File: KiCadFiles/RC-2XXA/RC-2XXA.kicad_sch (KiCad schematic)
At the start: 282 parts

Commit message: Refactor KiCad project files for RC-2XXA: streamline net connections in PCB, adjust solder mask clearance in project settings, and add new connector symbols in schematic. Enhance error handling for undefined net classes.
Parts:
- removed D1, D10, D11, D12, D13, D14, D15, D16, D17, D18, D19, D2, D20, D21, D22, D23, D24, D3, D4, D43, D44, D45, D5, D6, D66, D67, D68, D7, D8, D9, D90, D91, D92: 1N4148, Diode_SMD:D_SOD-323_HandSoldering, symbol Device:D
- removed MX1, MX10, MX11, MX12, MX13, MX14, MX15, MX16, MX17, MX18, MX19, MX2, MX20, MX21, MX22, MX23, MX24, MX3, MX4, MX43, MX44, MX45, MX5, MX6, MX66, MX67, MX68, MX7, MX8, MX9, MX90, MX91, MX92: MX_SW_solder, My-Fi Footprints:SW_MX_1u, symbol PCM_marbastlib-mx:MX_SW_solder
- added C1: 4.7n, Capacitor_SMD:C_0402_1005Metric, symbol Device:C_Small
- added C10 (x2): 1uF, Capacitor_SMD:C_0402_1005Metric, symbol Device:C_Small
- added C11: 4.7uF/10V, Capacitor_SMD:C_0402_1005Metric, symbol Device:C_Small
- added C12: 100nF, Capacitor_SMD:C_0402_1005Metric, symbol Device:C_Small
- added C2, C3, C4, C5, C6: 100nF, Capacitor_SMD:C_0402_1005Metric, symbol Device:C
- added C7: 10uF, Capacitor_SMD:C_0402_1005Metric, symbol Device:C
- added C8, C9: 1uF, Capacitor_SMD:C_0402_1005Metric, symbol Device:C
- added F1: 500mA, Fuse:Fuse_1206_3216Metric, symbol Device:Polyfuse_Small
- added J1: Conn_01x04_Pin, Connector_JST:JST_SH_SM04B-SRSS-TB_1x04-1MP_P1.00mm_Horizontal, symbol Connector:Conn_01x04_Pin
- added J2: Conn_01x01_Pin, TestPoint:TestPoint_THTPad_2.0x2.0mm_Drill1.0mm, symbol Connector:Conn_01x01_Pin
- added LED1, LED2, LED4, LED6: LED, My-Fi Footprints:DIP_LED_MX_3mm, symbol Device:LED
- added LED3, LED5: LED, My-Fi Footprints:CAPS_LED_MX_3mm, symbol Device:LED
- added R1: 1M, Resistor_SMD:R_0402_1005Metric, symbol Device:R_Small
- added R2, R3, R4, R6: 220, Resistor_SMD:R_0402_1005Metric, symbol Device:R_Small
- added R5, R8: 10k, Resistor_SMD:R_0402_1005Metric, symbol Device:R
- added R9: 39R, Resistor_SMD:R_0402_1005Metric, symbol Device:R
- added SW1, SW2: SW_DPST_x2, Button_Switch_SMD:SW_Push_1P1T_XKB_TS-1187A, symbol Switch:SW_DPST_x2
- added U1: SRV05-4, Package_TO_SOT_SMD:SOT-23-6, symbol Power_Protection:SRV05-4
- added U2: STM32F072CBTx, Package_QFP:LQFP-48_7x7mm_P0.5mm, symbol MCU_ST_STM32F0:STM32F072CBTx
- added U3: XC6206PxxxMR, Package_TO_SOT_SMD:SOT-23-3, symbol Regulator_Linear:XC6206PxxxMR
- added U4: TLV74318PDBVR, Package_TO_SOT_SMD:SOT-23-5, symbol pmw3360:TLV74318PDBVR
- added U5: PMW3360DM-T2QU, Library:TrackballHolder_34mm, symbol pmw3360:PMW3360DM-T2QU
- D1: renamed from D25; footprint Diode_SMD:D_SOD-323_HandSoldering -> Diode_SMD:D_SOD-123
- D10: renamed from D34; footprint Diode_SMD:D_SOD-323_HandSoldering -> Diode_SMD:D_SOD-123
- D100: renamed from D133; footprint Diode_SMD:D_SOD-323_HandSoldering -> Diode_SMD:D_SOD-123
- D101: renamed from D134; footprint Diode_SMD:D_SOD-323_HandSoldering -> Diode_SMD:D_SOD-123
- D102: renamed from D135; footprint Diode_SMD:D_SOD-323_HandSoldering -> Diode_SMD:D_SOD-123
- D103: renamed from D136; footprint Diode_SMD:D_SOD-323_HandSoldering -> Diode_SMD:D_SOD-123
- D104: renamed from D137; footprint Diode_SMD:D_SOD-323_HandSoldering -> Diode_SMD:D_SOD-123
- D11: renamed from D35; footprint Diode_SMD:D_SOD-323_HandSoldering -> Diode_SMD:D_SOD-123
- D12: renamed from D36; footprint Diode_SMD:D_SOD-323_HandSoldering -> Diode_SMD:D_SOD-123
- D13: renamed from D37; footprint Diode_SMD:D_SOD-323_HandSoldering -> Diode_SMD:D_SOD-123
- D14: renamed from D38; footprint Diode_SMD:D_SOD-323_HandSoldering -> Diode_SMD:D_SOD-123
- D15: renamed from D39; footprint Diode_SMD:D_SOD-323_HandSoldering -> Diode_SMD:D_SOD-123
- D16: renamed from D40; footprint Diode_SMD:D_SOD-323_HandSoldering -> Diode_SMD:D_SOD-123
- D17: renamed from D41; footprint Diode_SMD:D_SOD-323_HandSoldering -> Diode_SMD:D_SOD-123
- D18: renamed from D42; footprint Diode_SMD:D_SOD-323_HandSoldering -> Diode_SMD:D_SOD-123
- D19: renamed from D46; footprint Diode_SMD:D_SOD-323_HandSoldering -> Diode_SMD:D_SOD-123
- D2: renamed from D26; footprint Diode_SMD:D_SOD-323_HandSoldering -> Diode_SMD:D_SOD-123
- D20: renamed from D47; footprint Diode_SMD:D_SOD-323_HandSoldering -> Diode_SMD:D_SOD-123
- D21: renamed from D48; footprint Diode_SMD:D_SOD-323_HandSoldering -> Diode_SMD:D_SOD-123
- D22: renamed from D49; footprint Diode_SMD:D_SOD-323_HandSoldering -> Diode_SMD:D_SOD-123
- D23: renamed from D50; footprint Diode_SMD:D_SOD-323_HandSoldering -> Diode_SMD:D_SOD-123
- D24: renamed from D51; footprint Diode_SMD:D_SOD-323_HandSoldering -> Diode_SMD:D_SOD-123
- D25: renamed from D52; footprint Diode_SMD:D_SOD-323_HandSoldering -> Diode_SMD:D_SOD-123
- D26: renamed from D53; footprint Diode_SMD:D_SOD-323_HandSoldering -> Diode_SMD:D_SOD-123
- D27: renamed from D54; footprint Diode_SMD:D_SOD-323_HandSoldering -> Diode_SMD:D_SOD-123
- D28: renamed from D55; footprint Diode_SMD:D_SOD-323_HandSoldering -> Diode_SMD:D_SOD-123
- D29: renamed from D56; footprint Diode_SMD:D_SOD-323_HandSoldering -> Diode_SMD:D_SOD-123
- D3: renamed from D27; footprint Diode_SMD:D_SOD-323_HandSoldering -> Diode_SMD:D_SOD-123
- D30: renamed from D57; footprint Diode_SMD:D_SOD-323_HandSoldering -> Diode_SMD:D_SOD-123
- D31: renamed from D58; footprint Diode_SMD:D_SOD-323_HandSoldering -> Diode_SMD:D_SOD-123
- D32: renamed from D59; footprint Diode_SMD:D_SOD-323_HandSoldering -> Diode_SMD:D_SOD-123
- D33: renamed from D60; footprint Diode_SMD:D_SOD-323_HandSoldering -> Diode_SMD:D_SOD-123
- D34: renamed from D61; footprint Diode_SMD:D_SOD-323_HandSoldering -> Diode_SMD:D_SOD-123
- D35: renamed from D62; footprint Diode_SMD:D_SOD-323_HandSoldering -> Diode_SMD:D_SOD-123
- D36: renamed from D63; footprint Diode_SMD:D_SOD-323_HandSoldering -> Diode_SMD:D_SOD-123
- D37: renamed from D64; footprint Diode_SMD:D_SOD-323_HandSoldering -> Diode_SMD:D_SOD-123
- D38: renamed from D65; footprint Diode_SMD:D_SOD-323_HandSoldering -> Diode_SMD:D_SOD-123
- D39: renamed from D69; footprint Diode_SMD:D_SOD-323_HandSoldering -> Diode_SMD:D_SOD-123
- D4: renamed from D28; footprint Diode_SMD:D_SOD-323_HandSoldering -> Diode_SMD:D_SOD-123
- D40: renamed from D70; footprint Diode_SMD:D_SOD-323_HandSoldering -> Diode_SMD:D_SOD-123
- D41: renamed from D71; footprint Diode_SMD:D_SOD-323_HandSoldering -> Diode_SMD:D_SOD-123
- D42: renamed from D72; footprint Diode_SMD:D_SOD-323_HandSoldering -> Diode_SMD:D_SOD-123
- D43: renamed from D73; footprint Diode_SMD:D_SOD-323_HandSoldering -> Diode_SMD:D_SOD-123
- D44: renamed from D74; footprint Diode_SMD:D_SOD-323_HandSoldering -> Diode_SMD:D_SOD-123
- D45: renamed from D75; footprint Diode_SMD:D_SOD-323_HandSoldering -> Diode_SMD:D_SOD-123
- D46: renamed from D76; footprint Diode_SMD:D_SOD-323_HandSoldering -> Diode_SMD:D_SOD-123
- D47: renamed from D77; footprint Diode_SMD:D_SOD-323_HandSoldering -> Diode_SMD:D_SOD-123
- D48: renamed from D78; footprint Diode_SMD:D_SOD-323_HandSoldering -> Diode_SMD:D_SOD-123
- D49: renamed from D79; footprint Diode_SMD:D_SOD-323_HandSoldering -> Diode_SMD:D_SOD-123
- D5: renamed from D29; footprint Diode_SMD:D_SOD-323_HandSoldering -> Diode_SMD:D_SOD-123
- D50: renamed from D80; footprint Diode_SMD:D_SOD-323_HandSoldering -> Diode_SMD:D_SOD-123
- D51: renamed from D81; footprint Diode_SMD:D_SOD-323_HandSoldering -> Diode_SMD:D_SOD-123
- D52: renamed from D82; footprint Diode_SMD:D_SOD-323_HandSoldering -> Diode_SMD:D_SOD-123
- D53: renamed from D83; footprint Diode_SMD:D_SOD-323_HandSoldering -> Diode_SMD:D_SOD-123
- D54: renamed from D84; footprint Diode_SMD:D_SOD-323_HandSoldering -> Diode_SMD:D_SOD-123
- D55: renamed from D85; footprint Diode_SMD:D_SOD-323_HandSoldering -> Diode_SMD:D_SOD-123
- D56: renamed from D86; footprint Diode_SMD:D_SOD-323_HandSoldering -> Diode_SMD:D_SOD-123
- D57: renamed from D87; footprint Diode_SMD:D_SOD-323_HandSoldering -> Diode_SMD:D_SOD-123
- D58: renamed from D88; footprint Diode_SMD:D_SOD-323_HandSoldering -> Diode_SMD:D_SOD-123
- D59: renamed from D89; footprint Diode_SMD:D_SOD-323_HandSoldering -> Diode_SMD:D_SOD-123
- D6: renamed from D30; footprint Diode_SMD:D_SOD-323_HandSoldering -> Diode_SMD:D_SOD-123
- D60: renamed from D93; footprint Diode_SMD:D_SOD-323_HandSoldering -> Diode_SMD:D_SOD-123
- D61: renamed from D94; footprint Diode_SMD:D_SOD-323_HandSoldering -> Diode_SMD:D_SOD-123
- D62: renamed from D95; footprint Diode_SMD:D_SOD-323_HandSoldering -> Diode_SMD:D_SOD-123
- D63: renamed from D96; footprint Diode_SMD:D_SOD-323_HandSoldering -> Diode_SMD:D_SOD-123
- D64: renamed from D97; footprint Diode_SMD:D_SOD-323_HandSoldering -> Diode_SMD:D_SOD-123
- D65: renamed from D98; footprint Diode_SMD:D_SOD-323_HandSoldering -> Diode_SMD:D_SOD-123
- D66: renamed from D99; footprint Diode_SMD:D_SOD-323_HandSoldering -> Diode_SMD:D_SOD-123
- D67: renamed from D100; footprint Diode_SMD:D_SOD-323_HandSoldering -> Diode_SMD:D_SOD-123
- D68: renamed from D101; footprint Diode_SMD:D_SOD-323_HandSoldering -> Diode_SMD:D_SOD-123
- D69: renamed from D102; footprint Diode_SMD:D_SOD-323_HandSoldering -> Diode_SMD:D_SOD-123
- D7: renamed from D31; footprint Diode_SMD:D_SOD-323_HandSoldering -> Diode_SMD:D_SOD-123
- D70: renamed from D103; footprint Diode_SMD:D_SOD-323_HandSoldering -> Diode_SMD:D_SOD-123
- D71: renamed from D104; footprint Diode_SMD:D_SOD-323_HandSoldering -> Diode_SMD:D_SOD-123
- D72: renamed from D105; footprint Diode_SMD:D_SOD-323_HandSoldering -> Diode_SMD:D_SOD-123
- D73: renamed from D106; footprint Diode_SMD:D_SOD-323_HandSoldering -> Diode_SMD:D_SOD-123
- D74: renamed from D107; footprint Diode_SMD:D_SOD-323_HandSoldering -> Diode_SMD:D_SOD-123
- D75: renamed from D108; footprint Diode_SMD:D_SOD-323_HandSoldering -> Diode_SMD:D_SOD-123
- D76: renamed from D109; footprint Diode_SMD:D_SOD-323_HandSoldering -> Diode_SMD:D_SOD-123
- D77: renamed from D110; footprint Diode_SMD:D_SOD-323_HandSoldering -> Diode_SMD:D_SOD-123
- D78: renamed from D111; footprint Diode_SMD:D_SOD-323_HandSoldering -> Diode_SMD:D_SOD-123
- D79: renamed from D112; footprint Diode_SMD:D_SOD-323_HandSoldering -> Diode_SMD:D_SOD-123
- D8: renamed from D32; footprint Diode_SMD:D_SOD-323_HandSoldering -> Diode_SMD:D_SOD-123
- D80: renamed from D113; footprint Diode_SMD:D_SOD-323_HandSoldering -> Diode_SMD:D_SOD-123
- D81: renamed from D114; footprint Diode_SMD:D_SOD-323_HandSoldering -> Diode_SMD:D_SOD-123
- D82: renamed from D115; footprint Diode_SMD:D_SOD-323_HandSoldering -> Diode_SMD:D_SOD-123
- D83: renamed from D116; footprint Diode_SMD:D_SOD-323_HandSoldering -> Diode_SMD:D_SOD-123
- D84: renamed from D117; footprint Diode_SMD:D_SOD-323_HandSoldering -> Diode_SMD:D_SOD-123
- D85: renamed from D118; footprint Diode_SMD:D_SOD-323_HandSoldering -> Diode_SMD:D_SOD-123
- D86: renamed from D119; footprint Diode_SMD:D_SOD-323_HandSoldering -> Diode_SMD:D_SOD-123
- D87: renamed from D120; footprint Diode_SMD:D_SOD-323_HandSoldering -> Diode_SMD:D_SOD-123
- D88: renamed from D121; footprint Diode_SMD:D_SOD-323_HandSoldering -> Diode_SMD:D_SOD-123
- D89: renamed from D122; footprint Diode_SMD:D_SOD-323_HandSoldering -> Diode_SMD:D_SOD-123
- D9: renamed from D33; footprint Diode_SMD:D_SOD-323_HandSoldering -> Diode_SMD:D_SOD-123
- D90: renamed from D123; footprint Diode_SMD:D_SOD-323_HandSoldering -> Diode_SMD:D_SOD-123
- D91: renamed from D124; footprint Diode_SMD:D_SOD-323_HandSoldering -> Diode_SMD:D_SOD-123
- D92: renamed from D125; footprint Diode_SMD:D_SOD-323_HandSoldering -> Diode_SMD:D_SOD-123
- D93: renamed from D126; footprint Diode_SMD:D_SOD-323_HandSoldering -> Diode_SMD:D_SOD-123
- D94: renamed from D127; footprint Diode_SMD:D_SOD-323_HandSoldering -> Diode_SMD:D_SOD-123
- D95: renamed from D128; footprint Diode_SMD:D_SOD-323_HandSoldering -> Diode_SMD:D_SOD-123
- D96: renamed from D129; footprint Diode_SMD:D_SOD-323_HandSoldering -> Diode_SMD:D_SOD-123
- D97: renamed from D130; footprint Diode_SMD:D_SOD-323_HandSoldering -> Diode_SMD:D_SOD-123
- D98: renamed from D131; footprint Diode_SMD:D_SOD-323_HandSoldering -> Diode_SMD:D_SOD-123
- D99: renamed from D132; footprint Diode_SMD:D_SOD-323_HandSoldering -> Diode_SMD:D_SOD-123
- renumbered MX25 to MX1, MX34 to MX10, MX133 to MX100, MX134 to MX101, MX135 to MX102, MX136 to MX103, MX137 to MX104, MX35 to MX11, MX36 to MX12, MX37 to MX13, MX38 to MX14, MX39 to MX15, MX40 to MX16, MX41 to MX17, MX42 to MX18, MX46 to MX19, MX26 to MX2, MX47 to MX20, MX48 to MX21, MX49 to MX22, MX50 to MX23, MX51 to MX24, MX52 to MX25, MX53 to MX26, MX54 to MX27, MX55 to MX28, MX56 to MX29, MX27 to MX3, MX57 to MX30, MX58 to MX31, MX59 to MX32, MX60 to MX33, MX61 to MX34, MX62 to MX35, MX63 to MX36, MX64 to MX37, MX65 to MX38, MX69 to MX39, MX28 to MX4, MX70 to MX40, MX71 to MX41, MX72 to MX42, MX73 to MX43, MX74 to MX44, MX75 to MX45, MX76 to MX46, MX77 to MX47, MX78 to MX48, MX79 to MX49, MX29 to MX5, MX80 to MX50, MX81 to MX51, MX82 to MX52, MX83 to MX53, MX84 to MX54, MX85 to MX55, MX86 to MX56, MX87 to MX57, MX88 to MX58, MX89 to MX59, MX30 to MX6, MX93 to MX60, MX94 to MX61, MX95 to MX62, MX96 to MX63, MX97 to MX64, MX98 to MX65, MX99 to MX66, MX100 to MX67, MX101 to MX68, MX102 to MX69, MX31 to MX7, MX103 to MX70, MX104 to MX71, MX105 to MX72, MX106 to MX73, MX107 to MX74, MX108 to MX75, MX109 to MX76, MX110 to MX77, MX111 to MX78, MX112 to MX79, MX32 to MX8, MX113 to MX80, MX114 to MX81, MX115 to MX82, MX116 to MX83, MX117 to MX84, MX118 to MX85, MX119 to MX86, MX120 to MX87, MX121 to MX88, MX122 to MX89, MX33 to MX9, MX123 to MX90, MX124 to MX91, MX125 to MX92, MX126 to MX93, MX127 to MX94, MX128 to MX95, MX129 to MX96, MX130 to MX97, MX131 to MX98, MX132 to MX99, S134 to S101, S41 to S17, S73 to S43, S89 to S59, S100 to S67, S113 to S80, S122 to S89, S127 to S94
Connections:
- net COL1: now reaches MX26.1
- net COL1: now also MX4.1, MX48.1, MX68.1, U2.21 (PB10)
- net COL16: now reaches MX83.1
- net COL16: now also MX98.1, U2.3 (PC14)
- net COL6: now reaches MX53.1
- net COL6: now also MX31.1, MX73.1, MX9.1, MX94.1, U2.13 (PA3)
- net COL0: now reaches MX3.1
- net COL0: now also MX25.1, MX46.1, MX66.1, MX92.1, U2.22 (PB11)
- net COL7: now reaches MX10.1
- net COL7: now also MX32.1, MX54.1, MX74.1, U2.28 (PB15)
- net COL10: now reaches MX57.1
- net COL10: now also MX13.1, MX35.1, MX77.1, U2.25 (PB12)
- net COL11: now reaches MX36.1
- net COL11: now also MX14.1, MX58.1, MX78.1, MX95.1, U2.12 (PA2)
- net COL3: now reaches MX28.1
- net COL3: now also MX50.1, MX6.1, MX70.1, MX93.1, U2.19 (PB1)
- net COL9: now reaches MX56.1
- net COL9: now also MX12.1, MX34.1, MX76.1, U2.26 (PB13)
- net COL12: now reaches MX59.1
- net COL12: now also MX15.1, MX37.1, MX79.1, U2.11 (PA1)
- net COL8: now reaches MX33.1
- net COL8: now also MX11.1, MX55.1, MX75.1, U2.27 (PB14)
- net COL19: now reaches MX102.1
- net COL19: now also MX20.1, MX40.1, MX61.1, MX86.1
- net COL13: now reaches MX96.1
- net COL13: now also MX16.1, MX38.1, MX81.1, U2.6 (PF1)
- net COL15: now reaches MX82.1
- net COL15: now also MX97.1, U2.4 (PC15)
- net COL21: now reaches MX22.1
- net COL21: now also MX104.1, MX42.1, MX43.1, MX63.1, MX88.1, MX89.1
- net COL18: now reaches MX100.1
- net COL18: now also MX19.1, MX39.1, MX60.1, MX85.1
- net COL17: now reaches MX99.1
- net COL17: now also MX84.1, U2.2 (PC13)
- net COL2: now reaches MX49.1
- net COL2: now also MX27.1, MX5.1, MX69.1, U2.20 (PB2)
- net COL5: now reaches MX72.1
- net COL5: now also MX30.1, MX52.1, MX8.1
- net COL4: now reaches MX29.1
- net COL4: now also MX51.1, MX7.1, MX71.1
- net COL20: now reaches MX87.1
- net COL20: now also MX103.1, MX21.1, MX41.1, MX62.1
- net COL14: now reaches MX18.1
- net COL14: now also U2.5 (PF0)
- new net: LED3.2 (A), LED4.2 (A), R4.2
- new net: LED1.2 (A), R2.2
- new net: C11.1, C12.1, U5.3 (VDDPIX)
- new net: LED5.2 (A), LED6.2 (A), R6.2
- new net: R9.1, U5.15 (LED_P)
- new net: LED2.2 (A), R3.2
- new net +3V3: C10.1, C3.1, C4.1, C5.1, C6.1, C7.1, C9.1, R8.1, SW2.2 (B), U2.1 (VBAT), U2.24 (VDD), U2.36 (VDDIO2), U2.48 (VDD), U2.9 (VDDA), U3.2 (VO), U4.1 (IN), U4.3 (EN), U5.5 (VDDIO)
- new net +5V: C8.1, F1.2, U1.5 (VP), U3.3 (VI)
- new net BOOT-1: R5.1, SW2.1 (A), U2.44 (BOOT0)
- new net CAPLED: R4.1, U2.18 (PB0)
- new net CS: U2.14 (PA4), U5.13 (~{CS})
- new net DN: J1.2 (Pin_2), U1.4 (IO3), U2.32 (PA11)
- new net DP: J1.3 (Pin_3), U1.6 (IO4), U2.33 (PA12)
- new net ESCLED: R2.1, U2.41 (PB5)
- new net GND: C1.2, C10.2, C10.2, C11.2, C12.2, C2.2, C3.2, C4.2, C5.2, C6.2, C7.2, C8.2, C9.2, J1.4 (Pin_4), LED1.1 (K), LED2.1 (K), LED3.1 (K), LED4.1 (K), LED5.1 (K), LED6.1 (K), R1.2, R5.2, SW1.2 (B), U1.2 (VN), U2.23 (VSS), U2.35 (VSS), U2.47 (VSS), U2.8 (VSSA), U3.1 (GND), U4.2 (GND), U5.8 (GND)
- new net GNDREF: C1.1, J2.1 (Pin_1), R1.1
- new net MISO: R8.2, U2.16 (PA6), U5.12 (MISO)
- new net MOSI: U2.17 (PA7), U5.11 (MOSI)
- new net NUMLED: R6.1
- new net ROW0: U2.37 (PA14)
- new net ROW1: U2.38 (PA15)
- new net ROW2: U2.39 (PB3)
- new net ROW3: U2.40 (PB4)
- new net RST-1: C2.1, SW1.1 (A), U2.7 (NRST)
- new net SCLK: U2.15 (PA5), U5.10 (SCLK)
- new net SCLLED: R3.1, U2.42 (PB6)
- new net VBUS: F1.1, J1.1 (Pin_1)
- new net VDD_TR: C10.1, R9.2, U4.5 (OUT), U5.4 (VDD)
- no-connect marks 0 -> 6
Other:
- note added: "Boot Switch"
- note added: "Capslock LED"
- note added: "Decoupling Capacitors"
- note added: "ESC LED"
- note added: "ESD Protect"
- note added: "Fuse"
- note added: "JST Connetor"
- note added: "MCU STM32F072CBT6"
- note added: "Regulator TLV74318PDBVR 3.3V-1.8V"
- note added: "Regulator XC6206 5V-3.3V"
- note added: "Reset Switch"
- note added: "SENSOR PMW3360DM-T2QU"
- note added: "ScollLock LED"
- note added: "Shielding"
- moved on the sheet: D1, D10, D100, D101, D102, D103, D104, D11, D12, D13, D14, D15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

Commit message: Update rectangle positions in RC-2XXA schematic to correct alignment and spacing. Adjust multiple rectangle coordinates for improved layout consistency.
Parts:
- removed R2: 220, Resistor_SMD:R_0402_1005Metric, symbol Device:R_Small
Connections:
- net COL21 is gone; now on net COL20: MX104.1, MX22.1, MX42.1, MX43.1, MX63.1, MX88.1, MX89.1
- net ESCLED is gone; now on net SCLLED: U2.41 (PB5)
- net COL0: now also U2.5 (PF0); no longer U2.22 (PB11)
- net COL1: now also U2.6 (PF1); no longer U2.21 (PB10)
- net COL10: now also U2.45 (PB8); no longer U2.25 (PB12)
- net COL11: now also U2.46 (PB9); no longer U2.12 (PA2)
- net COL12: now also MX1.1, MX2.1, U2.21 (PB10); no longer U2.11 (PA1)
- net COL13: now also MX23.1, MX24.1, U2.22 (PB11); no longer U2.6 (PF1)
- net COL14: now also MX44.1, MX45.1, MX82.1, MX97.1, U2.25 (PB12); no longer U2.5 (PF0)
- net COL15: now also MX64.1, MX65.1, MX83.1, MX98.1, U2.26 (PB13); no longer MX82.1, MX97.1, U2.4 (PC15)
- net COL16: now also MX84.1, MX90.1, MX91.1, MX99.1, U2.27 (PB14); no longer MX83.1, MX98.1, U2.3 (PC14)
- net COL17: now also MX100.1, MX19.1, MX39.1, MX60.1, MX85.1, U2.28 (PB15); no longer MX84.1, MX99.1, U2.2 (PC13)
- net COL18: now also MX102.1, MX20.1, MX40.1, MX61.1, MX86.1, U2.10 (PA0); no longer MX100.1, MX19.1, MX39.1, MX60.1, MX85.1
- net COL19: now also MX103.1, MX21.1, MX41.1, MX62.1, MX87.1, U2.11 (PA1); no longer MX102.1, MX20.1, MX40.1, MX61.1, MX86.1
- net COL2: now also U2.2 (PC13); no longer U2.20 (PB2)
- net COL20: now also U2.12 (PA2); no longer MX103.1, MX21.1, MX41.1, MX62.1, MX87.1
- net COL3: now also U2.3 (PC14); no longer U2.19 (PB1)
- net COL4: now also U2.4 (PC15)
- net COL5: now also U2.20 (PB2)
- net COL6: now also U2.39 (PB3); no longer U2.13 (PA3)
- net COL7: now also U2.40 (PB4); no longer U2.28 (PB15)
- net COL8: now also U2.42 (PB6); no longer U2.27 (PB14)
- net COL9: now also U2.43 (PB7); no longer U2.26 (PB13)
- net NUMLED: now also U2.19 (PB1)
- net ROW0: now also D1.1 (K), D23.1 (K), D44.1 (K), D64.1 (K), D90.1 (K), U2.13 (PA3); no longer U2.37 (PA14)
- net ROW1: now also D2.1 (K), D24.1 (K), D45.1 (K), D65.1 (K), D91.1 (K), U2.29 (PA8); no longer U2.38 (PA15)
- net ROW2: now also D10.1 (K), D11.1 (K), D12.1 (K), D13.1 (K), D14.1 (K), D15.1 (K), D16.1 (K), D17.1 (K), D18.1 (K), D19.1 (K), D20.1 (K), D21.1 (K), D22.1 (K), D3.1 (K), D4.1 (K), D5.1 (K), D6.1 (K), D7.1 (K), D8.1 (K), D9.1 (K), U2.30 (PA9); no longer U2.39 (PB3)
- net ROW3: now also D25.1 (K), D26.1 (K), D27.1 (K), D28.1 (K), D29.1 (K), D30.1 (K), D31.1 (K), D32.1 (K), D33.1 (K), D34.1 (K), D35.1 (K), D36.1 (K), D37.1 (K), D38.1 (K), D39.1 (K), D40.1 (K), D41.1 (K), D42.1 (K), U2.31 (PA10); no longer U2.40 (PB4)
- net SCLLED: no longer U2.42 (PB6)
- net ROW6: now reaches D96.1 (K)
- net ROW6: now also D100.1 (K), D101.1 (K), D102.1 (K), D103.1 (K), D104.1 (K), D92.1 (K), D93.1 (K), D94.1 (K), D95.1 (K), D97.1 (K), D98.1 (K), D99.1 (K), U2.38 (PA15)
- net at LED1.2 (A): now also LED2.2 (A), R3.2
- net ROW4: now reaches U2.34 (PA13)
- net ROW4: now also D46.1 (K), D47.1 (K), D48.1 (K), D49.1 (K), D50.1 (K), D51.1 (K), D52.1 (K), D53.1 (K), D54.1 (K), D55.1 (K), D56.1 (K), D57.1 (K), D58.1 (K), D59.1 (K), D60.1 (K), D61.1 (K), D62.1 (K), D63.1 (K)
- net ROW5: now reaches D86.1 (K)
- net ROW5: now also D66.1 (K), D67.1 (K), D68.1 (K), D69.1 (K), D70.1 (K), D71.1 (K), D72.1 (K), D73.1 (K), D74.1 (K), D75.1 (K), D76.1 (K), D77.1 (K), D78.1 (K), D79.1 (K), D80.1 (K), D81.1 (K), D82.1 (K), D83.1 (K), D84.1 (K), D85.1 (K), D87.1 (K), D88.1 (K), U2.37 (PA14)
- no-connect marks 6 -> 5
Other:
- note removed: "ESC LED"
- moved on the sheet: D1, D10, D100, D101, D102, D103, D104, D11, D12, D13, D14, D15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

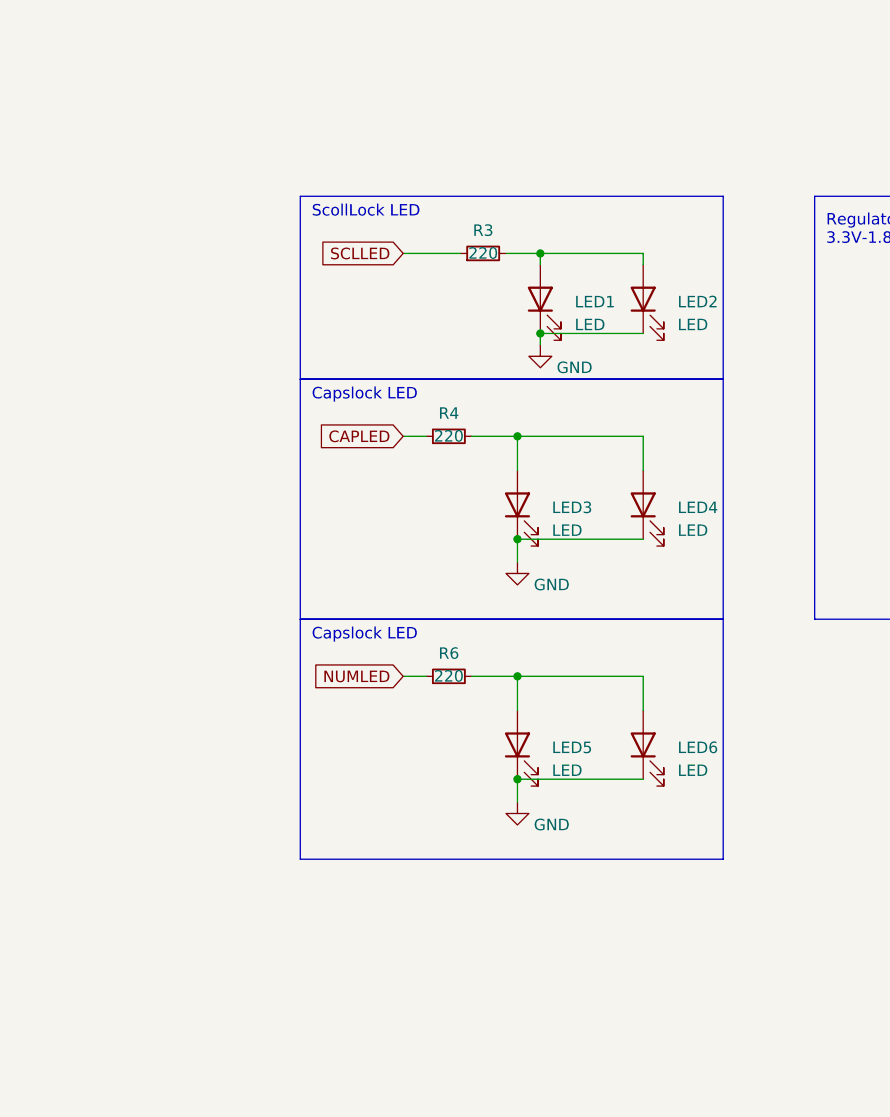
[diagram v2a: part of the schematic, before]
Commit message: Update RC-2XXA KiCad files: adjust footprint properties, correct rectangle positions in schematic, and enhance error handling for pin connections. Remove unnecessary junctions and wires for improved clarity.
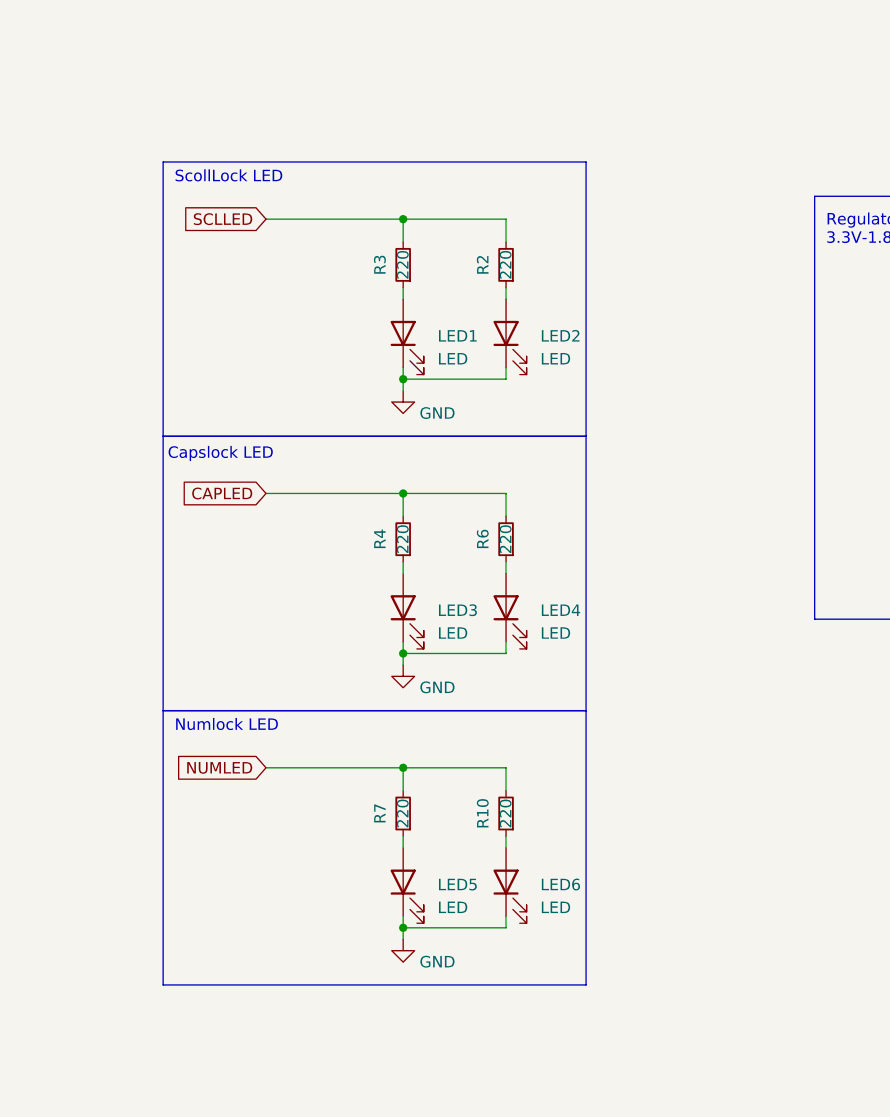
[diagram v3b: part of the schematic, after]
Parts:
- added R10, R2, R7: 220, Resistor_SMD:R_0402_1005Metric, symbol Device:R_Small
- LED3, LED5: footprint My-Fi Footprints:CAPS_LED_MX_3mm -> My-Fi Footprints:DIP_LED_MX_3mm
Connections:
- net CAPLED: now also R4.2, R6.2; no longer R4.1
- net NUMLED: now also R10.2, R7.2; no longer R6.1
- net SCLLED: now also R3.2, R2.2; no longer R3.1
- new net: LED4.2 (A), R6.1
- new net: LED5.2 (A), R7.1
- new net: LED3.2 (A), R4.1
- new net: LED1.2 (A), R3.1
- new net: LED6.2 (A), R10.1
- new net: LED2.2 (A), R2.1
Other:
- note added: "Numlock LED"
- moved on the sheet: LED1, LED2, R3

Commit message: Add Zener diode symbol to RC-2XXA schematic, update component references and footprints for capacitors and resistors, and correct wire connections for improved circuit clarity.
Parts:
- added D206: SMF6.0A, acheron_Components:D_SOD-123, symbol Device:D_Zener
- C1: value 4.7n -> 4.7nF; footprint Capacitor_SMD:C_0402_1005Metric -> Capacitor_SMD:C_0805_2012Metric_Pad1.18x1.45mm_HandSolder
- C10: renamed from C6; footprint Capacitor_SMD:C_0402_1005Metric -> Capacitor_SMD:C_0805_2012Metric_Pad1.18x1.45mm_HandSolder
- C11: renamed from C7; footprint Capacitor_SMD:C_0402_1005Metric -> Capacitor_SMD:C_0805_2012Metric_Pad1.18x1.45mm_HandSolder
- C12: renamed from C8; footprint Capacitor_SMD:C_0402_1005Metric -> Capacitor_SMD:C_0805_2012Metric_Pad1.18x1.45mm_HandSolder
- C13: renamed from C9; footprint Capacitor_SMD:C_0402_1005Metric -> Capacitor_SMD:C_0805_2012Metric_Pad1.18x1.45mm_HandSolder
- C2, C3: renamed from C10; footprint Capacitor_SMD:C_0402_1005Metric -> Capacitor_SMD:C_0805_2012Metric_Pad1.18x1.45mm_HandSolder
- C4: renamed from C11; footprint Capacitor_SMD:C_0402_1005Metric -> Capacitor_SMD:C_0805_2012Metric_Pad1.18x1.45mm_HandSolder
- C5: renamed from C12; footprint Capacitor_SMD:C_0402_1005Metric -> Capacitor_SMD:C_0805_2012Metric_Pad1.18x1.45mm_HandSolder
- C6: renamed from C2; footprint Capacitor_SMD:C_0402_1005Metric -> Capacitor_SMD:C_0805_2012Metric_Pad1.18x1.45mm_HandSolder
- C7: renamed from C3; footprint Capacitor_SMD:C_0402_1005Metric -> Capacitor_SMD:C_0805_2012Metric_Pad1.18x1.45mm_HandSolder
- C8: renamed from C4; footprint Capacitor_SMD:C_0402_1005Metric -> Capacitor_SMD:C_0805_2012Metric_Pad1.18x1.45mm_HandSolder
- C9: renamed from C5; footprint Capacitor_SMD:C_0402_1005Metric -> Capacitor_SMD:C_0805_2012Metric_Pad1.18x1.45mm_HandSolder
- R1: footprint Resistor_SMD:R_0402_1005Metric -> Resistor_SMD:R_0805_2012Metric_Pad1.20x1.40mm_HandSolder
- R10: renamed from R5; footprint Resistor_SMD:R_0402_1005Metric -> Resistor_SMD:R_0805_2012Metric_Pad1.20x1.40mm_HandSolder
- R2: renamed from R3; footprint Resistor_SMD:R_0402_1005Metric -> Resistor_SMD:R_0805_2012Metric_Pad1.20x1.40mm_HandSolder
- R3: renamed from R2; footprint Resistor_SMD:R_0402_1005Metric -> Resistor_SMD:R_0805_2012Metric_Pad1.20x1.40mm_HandSolder
- R4: renamed from R8; footprint Resistor_SMD:R_0402_1005Metric -> Resistor_SMD:R_0805_2012Metric_Pad1.20x1.40mm_HandSolder
- R5: renamed from R9; footprint Resistor_SMD:R_0402_1005Metric -> Resistor_SMD:R_0805_2012Metric_Pad1.20x1.40mm_HandSolder
- R6: renamed from R4; footprint Resistor_SMD:R_0402_1005Metric -> Resistor_SMD:R_0805_2012Metric_Pad1.20x1.40mm_HandSolder
- R7: renamed from R6; footprint Resistor_SMD:R_0402_1005Metric -> Resistor_SMD:R_0805_2012Metric_Pad1.20x1.40mm_HandSolder
- R8: renamed from R7; footprint Resistor_SMD:R_0402_1005Metric -> Resistor_SMD:R_0805_2012Metric_Pad1.20x1.40mm_HandSolder
- R9: renamed from R10; footprint Resistor_SMD:R_0402_1005Metric -> Resistor_SMD:R_0805_2012Metric_Pad1.20x1.40mm_HandSolder
- U2: renamed from U5; footprint Library:TrackballHolder_34mm -> My-Fi Footprints:TrackballHolder_34mm
- renumbered J2 to J1, J1 to J2, U4 to U1, U1 to U3, U2 to U4, U3 to U5
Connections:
- net +5V: now also D206.1 (K)
- net GND: now also D206.2 (A)

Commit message: updated pcb & sch
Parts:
- added D105: SMF9.0CA, acheron_Components:D_SOD-123_Bidirectional, symbol Device:D_TVS
- added J3: Conn_01x04_Pin, Connector_PinHeader_1.27mm:PinHeader_1x04_P1.27mm_Vertical, symbol Connector:Conn_01x04_Pin
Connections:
- net COL0: no longer U4.5 (PF0)
- net COL1: no longer U4.6 (PF1)
- net COL10: no longer U4.45 (PB8)
- net COL11: no longer U4.46 (PB9)
- net COL12: no longer U4.21 (PB10)
- net COL13: no longer U4.22 (PB11)
- net COL14: no longer U4.25 (PB12)
- net COL15: no longer U4.26 (PB13)
- net COL16: no longer U4.27 (PB14)
- net COL17: no longer U4.28 (PB15)
- net COL18: no longer U4.10 (PA0)
- net COL19: no longer U4.11 (PA1)
- net COL2: no longer U4.2 (PC13)
- net COL20: no longer U4.12 (PA2)
- net COL3: no longer U4.3 (PC14)
- net COL4: no longer U4.4 (PC15)
- net COL5: no longer U4.20 (PB2)
- net COL6: no longer U4.39 (PB3)
- net COL7: no longer U4.40 (PB4)
- net COL8: no longer U4.42 (PB6)
- net COL9: no longer U4.43 (PB7)
- net DN: now also J3.2 (Pin_2)
- net DP: now also J3.3 (Pin_3)
- net GND: now also J3.4 (Pin_4)
- net ROW0: no longer U4.13 (PA3)
- net ROW1: no longer U4.29 (PA8)
- net ROW2: no longer U4.30 (PA9)
- net ROW3: no longer U4.31 (PA10)
- net ROW4: no longer U4.34 (PA13)
- net ROW5: no longer U4.37 (PA14)
- net ROW6: no longer U4.38 (PA15)
- net VBUS: now also J3.1 (Pin_1)
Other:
- note added: "Cable Connetor"

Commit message: feat(kicad): sync RC-2XXA schematic/PCB and add routing presets
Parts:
- removed D101, D17, D43, D47, D67, D79, D89: 1N4148, Diode_SMD:D_SOD-123, symbol Device:D
- removed D105: SMF9.0CA, acheron_Components:D_SOD-123_Bidirectional, symbol Device:D_TVS
- removed U3: SRV05-4, Package_TO_SOT_SMD:SOT-23-6, symbol Power_Protection:SRV05-4
- added U3: TPD4E05U06DQAR, My-Fi Footprints:USON-10_2.5x1.0mm_P0.5mm, symbol Unified-Daughterboard-rescue:TPD4E05U06DQAR-acheronSymbols
- D1, D10, D100, D102, D103, D104, D11, D12, D13, D14, D15, D16, D18, D19, D2, D20, D21, D22, D23, D24, D25, D26, D27, D28, D29, D3, D30, D31, D32, D33, D34, D35, D36, D37, D38, D39, D4, D40, D41, D42, D44, D45, D46, D48, D49, D5, D50, D51, D52, D53, D54, D55, D56, D57, D58, D59, D6, D60, D61, D62, D63, D64, D65, D66, D68, D69, D7, D70, D71, D72, D73, D74, D75, D76, D77, D78, D8, D80, D81, D82, D83, D84, D85, D86, D87, D88, D9, D90, D91, D92, D93, D94, D95, D96, D97, D98, D99: footprint Diode_SMD:D_SOD-123 -> My-Fi Footprints:D_SOD-123-g
- D206: footprint acheron_Components:D_SOD-123 -> My-Fi Footprints:D_SOD-123
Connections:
- net COL0: now also MX47.1
- net COL1: now also MX67.1
- net COL12: now also MX80.1
- net COL13: now also MX17.1
- net COL17: now also MX101.1
- net DN: now also U3.2 (IO2), U3.5 (D2-), U3.6 (NC), U3.9 (NC)
- net DP: now also U3.1 (IO1), U3.10 (NC), U3.4 (D2+), U3.7 (NC)
- net GND: now also U3.3 (GND), U3.8 (GND)
- net at MX17.2: now also D16.2 (A), MX16.2
- net at MX101.2: now also D100.2 (A), MX100.2
- net at D46.2 (A), MX46.2: now also MX47.2
- net at D88.2 (A), MX88.2: now also MX89.2
- net at D68.2 (A), MX68.2: now also MX67.2
- net at MX79.2: now also D80.2 (A), MX80.2
- net at D42.2 (A), MX42.2: now also MX43.2
- no-connect marks 5 -> 3

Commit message: Refactor code structure for improved readability and maintainability
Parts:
- added J4, J5: Conn_01x07_Socket, Connector_JST:JST_SH_SM07B-SRSS-TB_1x07-1MP_P1.00mm_Horizontal, symbol Connector:Conn_01x07_Socket
- LED3: footprint My-Fi Footprints:DIP_LED_MX_3mm -> My-Fi Footprints:CAPS_LED_MX_3mm
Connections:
- net COL0: now also J4.5 (Pin_5)
- net COL1: now also J4.4 (Pin_4)
- net COL10: now also J5.2 (Pin_2)
- net COL11: now also J5.1 (Pin_1)
- net COL2: now also J4.3 (Pin_3)
- net COL3: now also J4.2 (Pin_2)
- net COL4: now also J4.1 (Pin_1)
- net COL5: now also J5.7 (Pin_7)
- net COL6: now also J5.6 (Pin_6)
- net COL7: now also J5.5 (Pin_5)
- net COL8: now also J5.4 (Pin_4)
- net COL9: now also J5.3 (Pin_3)
- net ROW0: now also J4.7 (Pin_7)
- net ROW1: now also J4.6 (Pin_6)
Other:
- note added: "F-Row-Connectors"
